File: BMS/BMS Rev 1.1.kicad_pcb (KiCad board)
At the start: 2 copper layers, 18 x 50.8 mm, 38 parts, among them J2 out, J3 out, J4 in, J5 in, Q1 CSD18502Q5B, Q2 CSD18502Q5B, U1 BQ41Z50RSNR

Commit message: Added everything
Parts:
- J3: moved to F.Cu
- moved REF** 36.5 mm to (149.9, 82.5), turned to 90 degrees
- moved REF** 36.4 mm to (149.9, 94.5), turned to 90 degrees
- moved JP3 35.7 mm to (149.7, 86.9), turned to 90 degrees
- moved JP4 35.7 mm to (149.7, 86.9), turned to 90 degrees
- moved JP2 35.7 mm to (149.7, 90.3), turned to 90 degrees
- moved JP1 35.7 mm to (149.7, 90.2), turned to 90 degrees
- moved J5 29.6 mm to (154.8, 94.4), turned to 90 degrees
- moved REF** 29.3 mm to (194.7, 82.5), turned to 90 degrees
- moved REF** 29.2 mm to (194.7, 94.5), turned to 90 degrees
- moved J3 28.1 mm to (194.8, 90.0), turned to 90 degrees
- moved J4 22.3 mm to (160.4, 82.5), turned to 0 degrees
- moved R6 19.9 mm to (161.3, 92.2), turned to 180 degrees
- moved D1 19.6 mm to (163.3, 96.1), turned to 0 degrees
- moved R8 19.5 mm to (188.7, 88.3), turned to -90 degrees
- moved R1 17.9 mm to (162.4, 86.6), turned to 90 degrees
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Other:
- board size 18 x 50.8 mm -> 50.9 x 18 mm

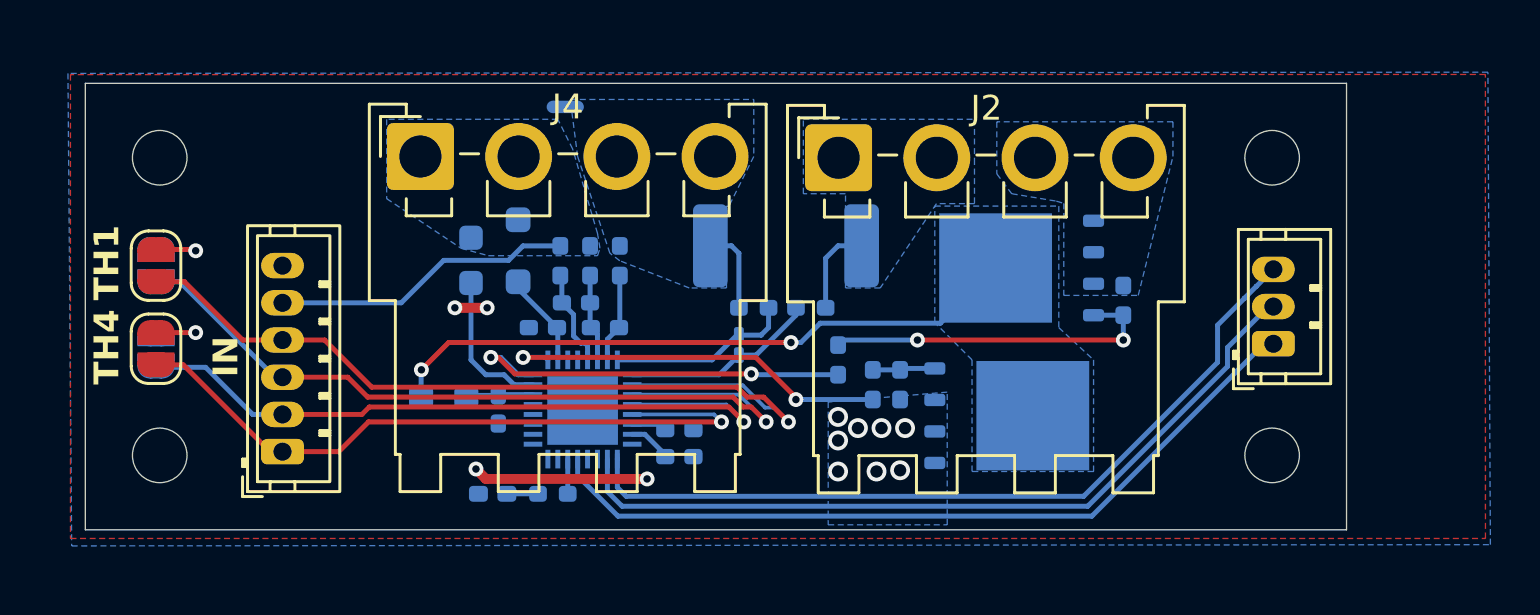
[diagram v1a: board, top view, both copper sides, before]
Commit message: Added BOMs and updated some PCB files
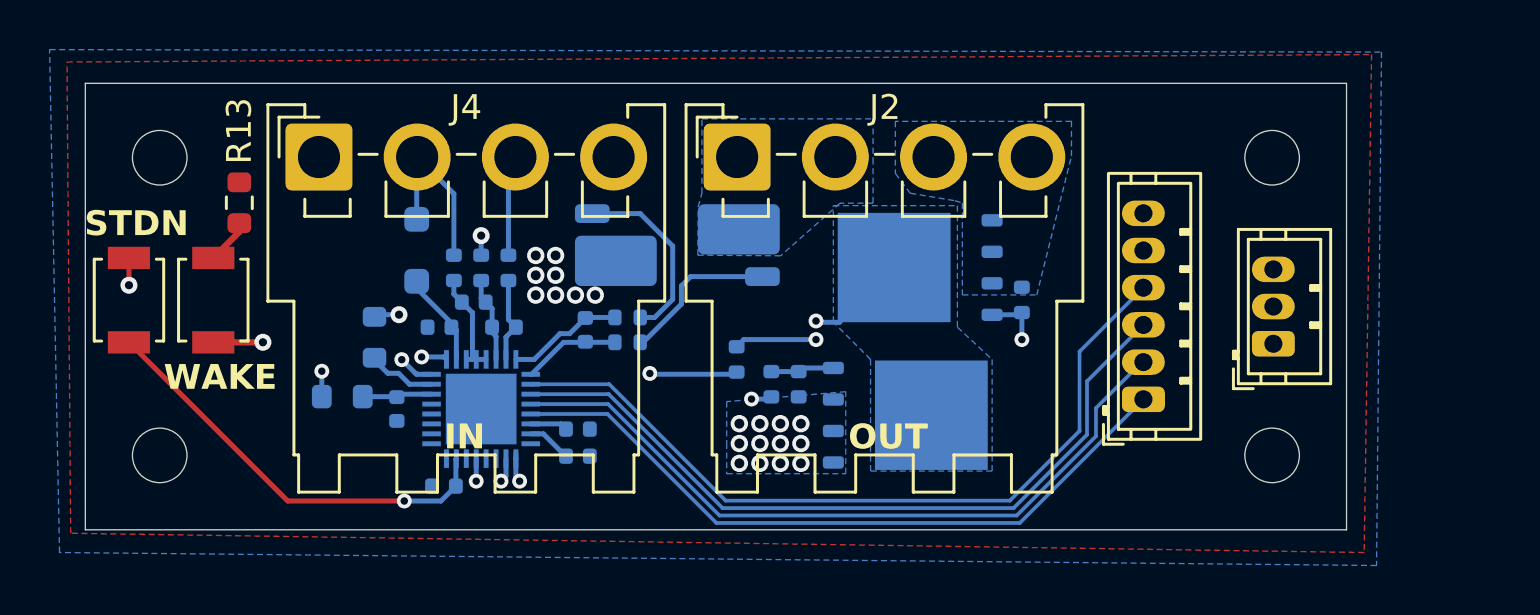
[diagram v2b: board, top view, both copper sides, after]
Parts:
- removed D1: LED, LED_SMD:LED_0402_1005Metric_Pad0.77x0.64mm_HandSolder
- removed JP1, JP2, JP3, JP4: SolderJumper_2_Open, Jumper:SolderJumper-2_P1.3mm_Open_RoundedPad1.0x1.5mm
- removed NT2: NetTie_2, NetTie:NetTie-2_SMD_Pad0.5mm
- added C8: 1nf, Capacitor_SMD:C_0402_1005Metric, B.Cu at (161.3, 95.8)
- added SW1: WAKE, Button_Switch_SMD:SW_SPST_B3U-1000P, F.Cu at (152.1, 88.2)
- added SW2: SHUTDN, Button_Switch_SMD:SW_SPST_B3U-1000P, F.Cu at (148.7, 88.2)
- C1, C2, C3, C4, C6, C7: footprint Capacitor_SMD:C_0402_1005Metric_Pad0.74x0.62mm_HandSolder -> Capacitor_SMD:C_0402_1005Metric
- C5: footprint Capacitor_SMD:C_0201_0603Metric_Pad0.64x0.40mm_HandSolder -> Capacitor_SMD:C_0402_1005Metric
- R1, R6: footprint Resistor_SMD:R_0603_1608Metric_Pad0.98x0.95mm_HandSolder -> Resistor_SMD:R_0603_1608Metric
- R10, R11, R12, R2, R3, R4, R7, R8, R9: footprint Resistor_SMD:R_0402_1005Metric_Pad0.72x0.64mm_HandSolder -> Resistor_SMD:R_0402_1005Metric
- R13: value 220 -> 10k; footprint Resistor_SMD:R_0402_1005Metric_Pad0.72x0.64mm_HandSolder -> Resistor_SMD:R_0603_1608Metric; moved to F.Cu
- R5: value 3m -> R_Shunt; footprint Resistor_SMD:R_2512_6332Metric_Pad1.40x3.35mm_HandSolder -> Resistor_SMD:R_Shunt_Vishay_WSK2512_6332Metric_T2.21mm
- moved J5 34.8 mm to (189.6, 92.2)
- moved R13 17.2 mm to (153.1, 84.3), turned to -90 degrees
- moved R10 7.52 mm to (168.8, 90.0)
- moved C5 6.22 mm to (167.1, 89.5)
- moved R11 5.10 mm to (168.8, 89.0), turned to 0 degrees
- moved R1 4.98 mm to (158.6, 89.8)
- moved R2 4.50 mm to (163.9, 87.0)
- moved R3 4.40 mm to (162.8, 87.0)
- moved R5 4.38 mm to (170.8, 86.0), turned to 0 degrees
- moved R4 4.30 mm to (161.8, 87.0)
- moved C2 4.17 mm to (161.2, 89.3)
- moved C3 4.12 mm to (162.6, 88.3)
- moved J2 4.09 mm to (173.2, 82.5)
- moved J4 4.09 mm to (156.3, 82.5)
- moved C4 4.09 mm to (159.4, 92.6)
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- renumbered U1 to IC1
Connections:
- IC1 pad 19: unconnected-(IC1-VC4-Pad19) -> Net-(IC1-VC2)
- IC1 pad 20: unconnected-(IC1-VC3-Pad20) -> Net-(IC1-VC2)
- IC1 pad 6: Net-(IC1-GPIO3) -> unconnected-(IC1-GPIO3-Pad6)
- IC1 pad 7: unconnected-(IC1-~{PRES}/_~{SHUTDN}-Pad7) -> Net-(IC1-~{PRES}/_~{SHUTDN})
- J4 pad 3: GNDPWR -> GND
- J4 pad 4: GNDPWR -> GND
- R1 pad 2: /B+ -> /B+ out
- R10 pad 2: /B- out -> Net-(R10-Pad2)
- R11 pad 2: GNDPWR -> Net-(R11-Pad2)
- R13 pad 1: Net-(D1-A) -> /B+
- R13 pad 2: Net-(IC1-GPIO3) -> Net-(R13-Pad2)
- R2 pad 2: GNDPWR -> GND
- R3 pad 2: /B+ -> /CELL1
- R4 pad 2: /CELL1 -> /B+
- R5 pad 1: /B- out -> GND
- R5 pad 2: GNDPWR -> Net-(R11-Pad2)
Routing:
- net /B+ out: track 0.10 -> 57.4 mm, vias 0 -> 2
- net Net-(IC1-~{PRES}/_~{SHUTDN}): track 0.00 -> 17.2 mm, vias 0 -> 1
- net /CELL1: track 12.2 -> 27.7 mm, vias 0 -> 1
- net /B+: track 0.00 -> 8.59 mm, vias 8 -> 12
- net Net-(R11-Pad2): track 0.00 -> 7.55 mm
- net Net-(R10-Pad2): track 0.00 -> 6.54 mm
- net GND: track 11.6 -> 5.43 mm, vias 6 -> 9
- net /SCL: track 32.2 -> 36.6 mm, vias 0 -> 1
- net /alert: track 32.3 -> 36.5 mm, vias 0 -> 1
- net Net-(IC1-SRN): track 7.90 -> 3.94 mm
- net /SDA: track 32.6 -> 36.5 mm, vias 0 -> 1
- net /B- out: track 3.66 -> 0.00 mm
- net GNDPWR: track 3.48 -> 0.00 mm
- net Net-(IC1-PACK): track 6.01 -> 2.71 mm
- net Net-(IC1-SRP): track 7.45 -> 4.69 mm
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- added copper zone on In1.Cu, net GND
- added copper zone on In2.Cu, net GND
- removed copper zone on B.Cu, net GNDPWR
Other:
- copper layers 2 -> 4
- board text added: "STDN"
- board text added: "WAKE"
- board text removed: "TH1"
- board text removed: "TH2"
- board text removed: "TH3"
- board text removed: "TH4"
